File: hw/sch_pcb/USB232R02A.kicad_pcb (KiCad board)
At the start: 2 copper layers, 40.1 x 30 mm, 38 parts, among them J1 USB_B, J10 -, J11 -, J12 -, J13 -, J14 -, J15 -, J16 -, J17 HEADER_2x01_PARALLEL, J2 HEADER_2x03_PARALLEL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

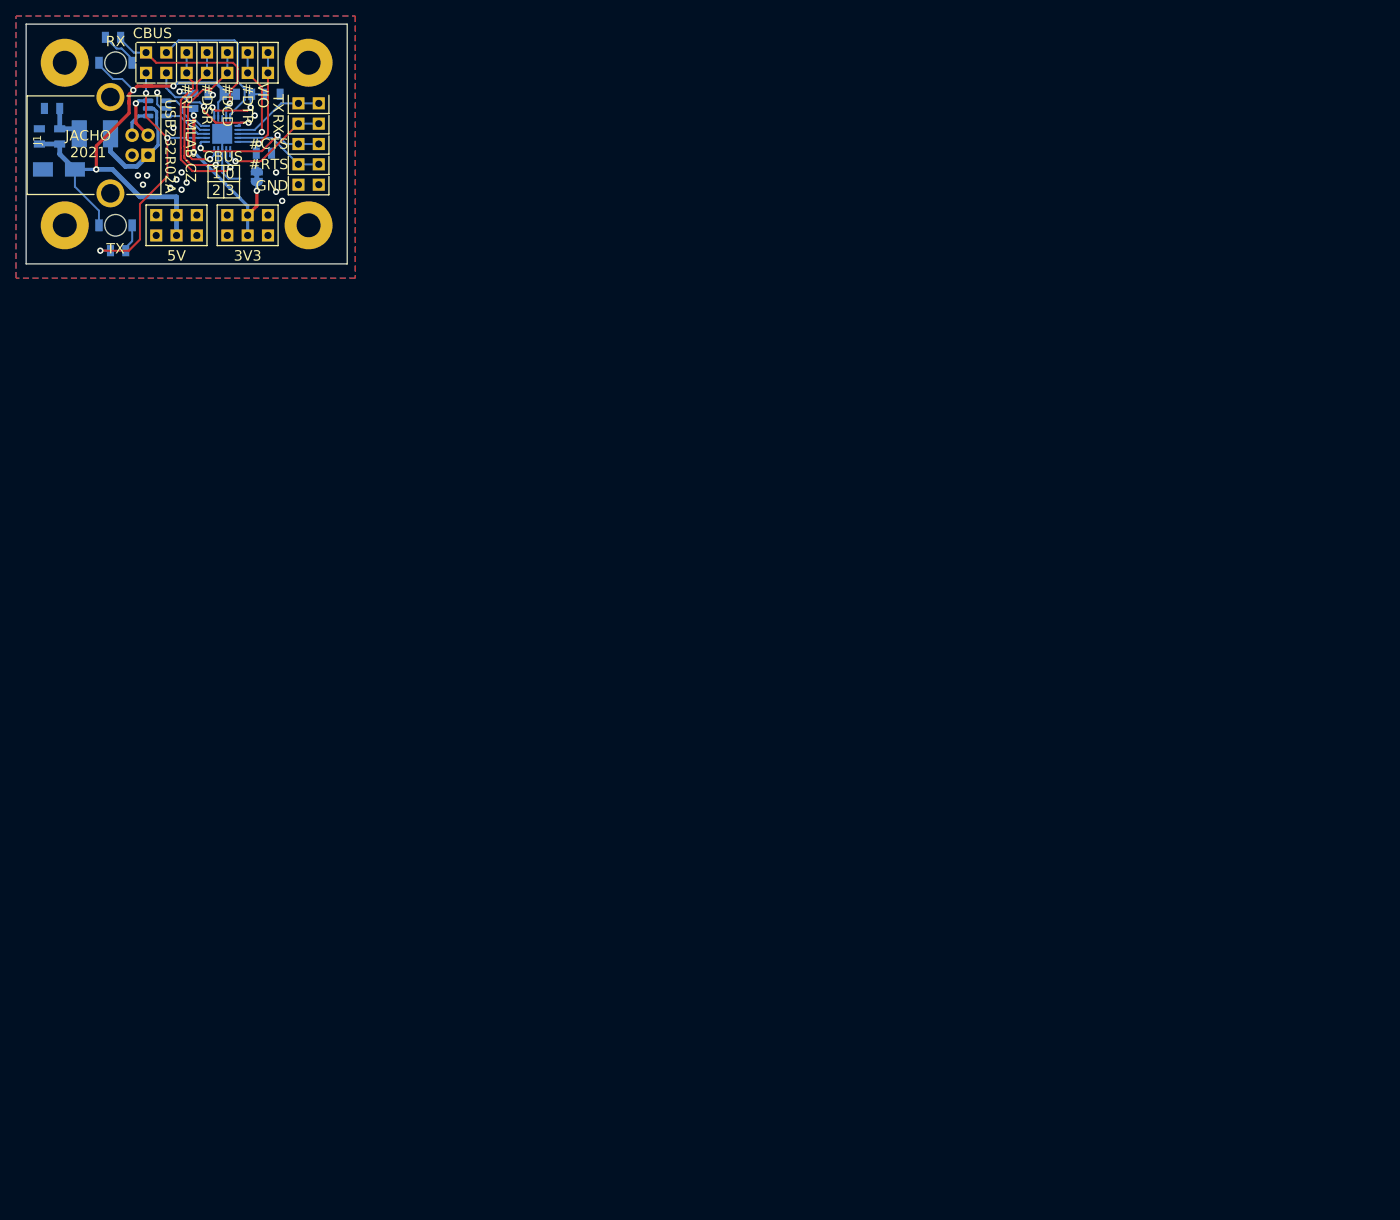
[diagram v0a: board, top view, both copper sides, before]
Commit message: vyreseni DRC, uprava sablon
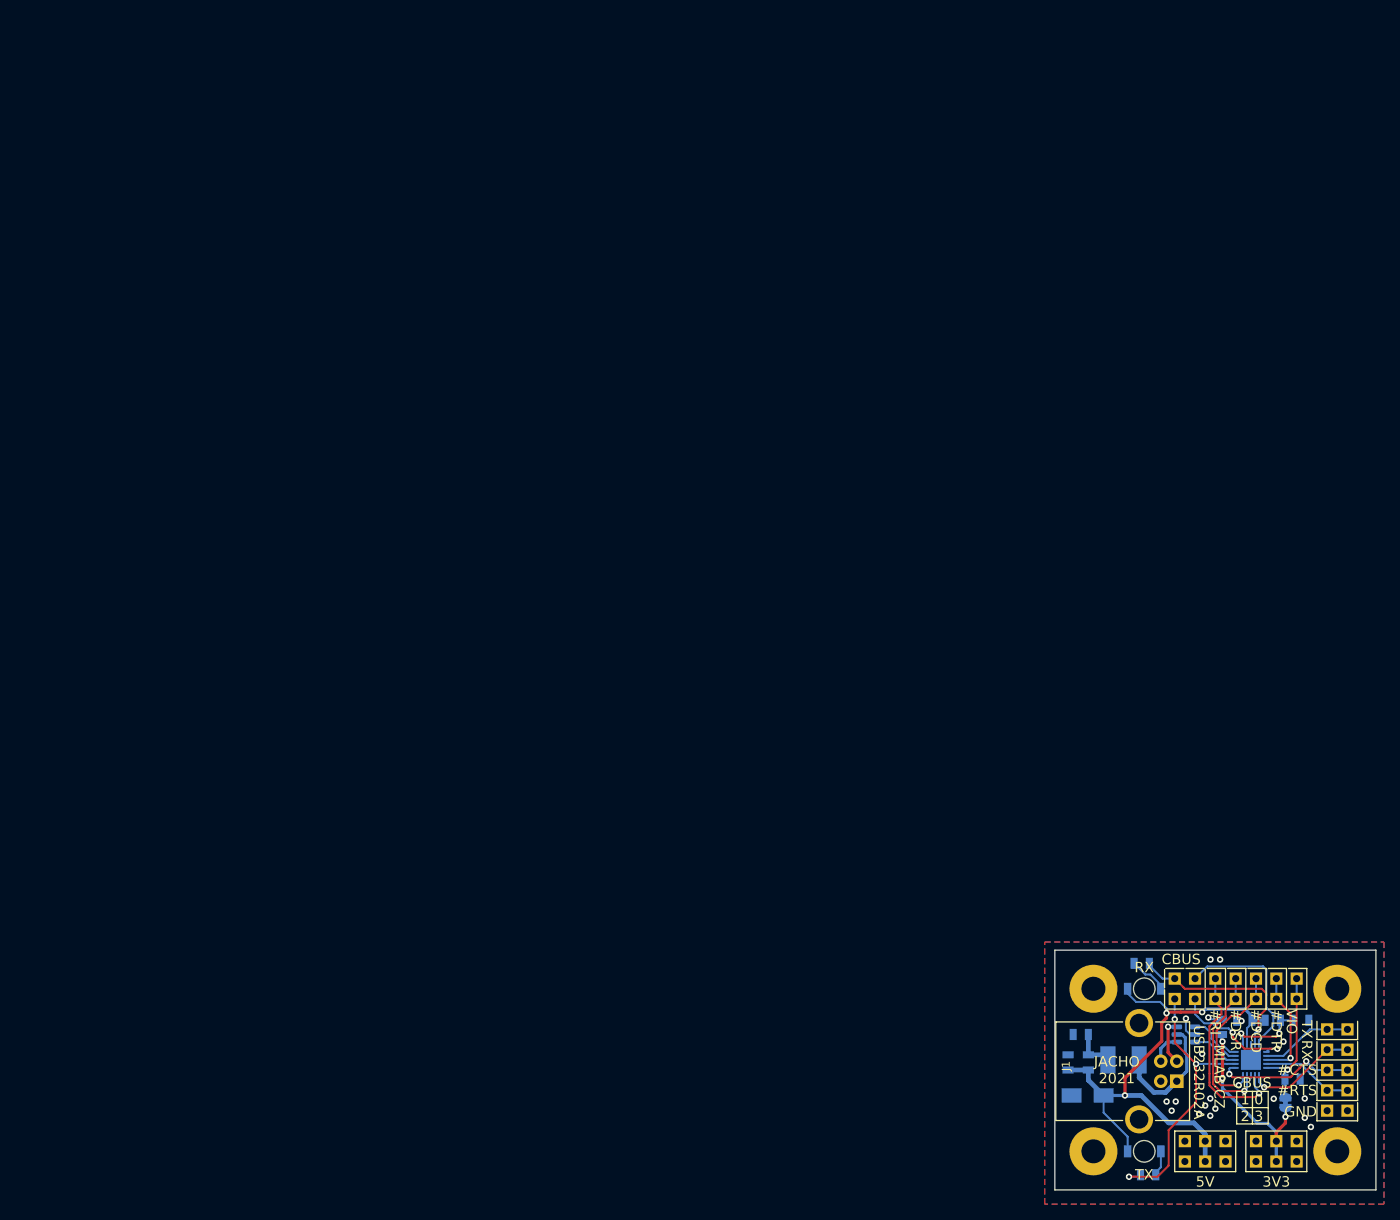
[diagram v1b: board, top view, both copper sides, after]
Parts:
- moved C3 173.0 mm to (149.7, 95.1)
- moved F1 173.0 mm to (137.4, 99.2)
- moved H4 173.0 mm to (164.1, 110.7)
- moved J1 173.0 mm to (144.1, 101.9)
- moved J13 173.0 mm to (146.4, 89.1)
- moved J3 173.0 mm to (156.5, 110.7)
- moved J6 173.0 mm to (164.1, 98.0)
- moved J7 173.0 mm to (164.1, 103.1)
- moved JP1 173.0 mm to (157.7, 104.6)
- moved C2 173.0 mm to (130.5, 99.6)
- moved D1 173.0 mm to (132.9, 103.7)
- moved FB1 173.0 mm to (133.0, 99.6)
- moved H1 173.0 mm to (164.1, 90.4)
- moved J11 173.0 mm to (154.0, 90.4)
- moved J12 173.0 mm to (148.9, 90.4)
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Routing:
- net GND: track 14.6 -> 7.16 mm, vias 16 -> 19
- net +5V: track 70.2 -> 68.8 mm
- net +3V3: track 26.2 -> 26.8 mm
- net /#DSR: track 21.3 -> 20.7 mm
- net /CBUS3: track 16.4 -> 15.8 mm

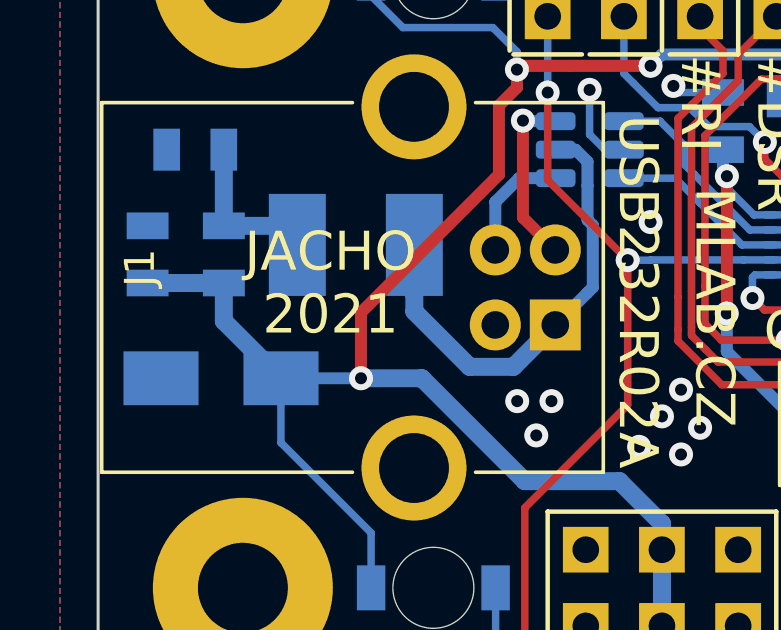
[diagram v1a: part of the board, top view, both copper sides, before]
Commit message: Úprava potisku
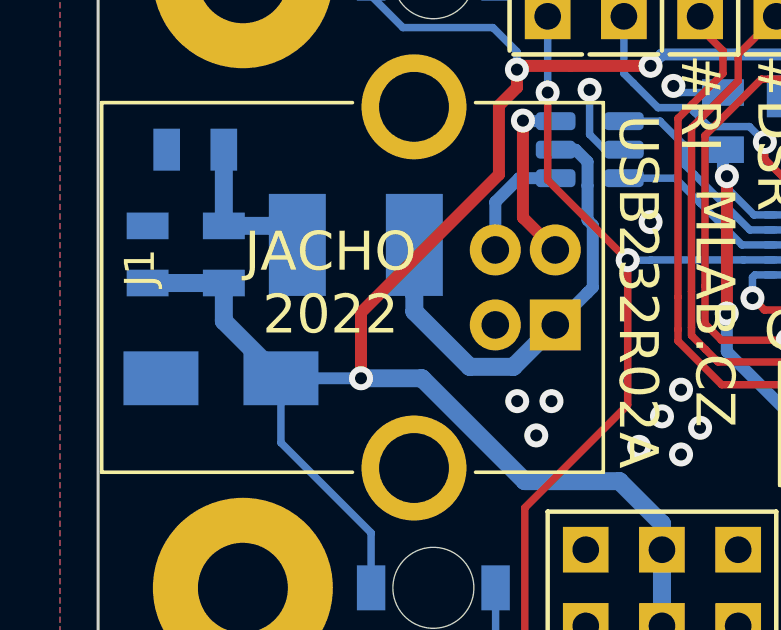
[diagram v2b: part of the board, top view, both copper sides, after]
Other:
- board text added: "JACHO 2022"
- board text removed: "JACHO 2021"
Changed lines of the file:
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@@
     (effects (font (size 1.3 1.3) (thickness 0.3)) (justify left))
   )
-  (gr_text "JACHO\n2021" (at 136.586 100.514) (layer "F.SilkS")
+  (gr_text "JACHO\n2022" (at 136.586 100.514) (layer "F.SilkS")
     (effects (font (size 1.3 1.3) (thickness 0.3)))
   )

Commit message: Swap mounting holes from top to bottom, to allow its use for aligment in PnP data output.
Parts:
- H1, H2, H3, H4: moved to B.Cu
- turned H1 to 180 degrees
- turned H2 to 180 degrees
- turned H3 to 180 degrees
- turned H4 to 180 degrees
